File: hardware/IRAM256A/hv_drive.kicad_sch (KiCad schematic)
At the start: 21 parts

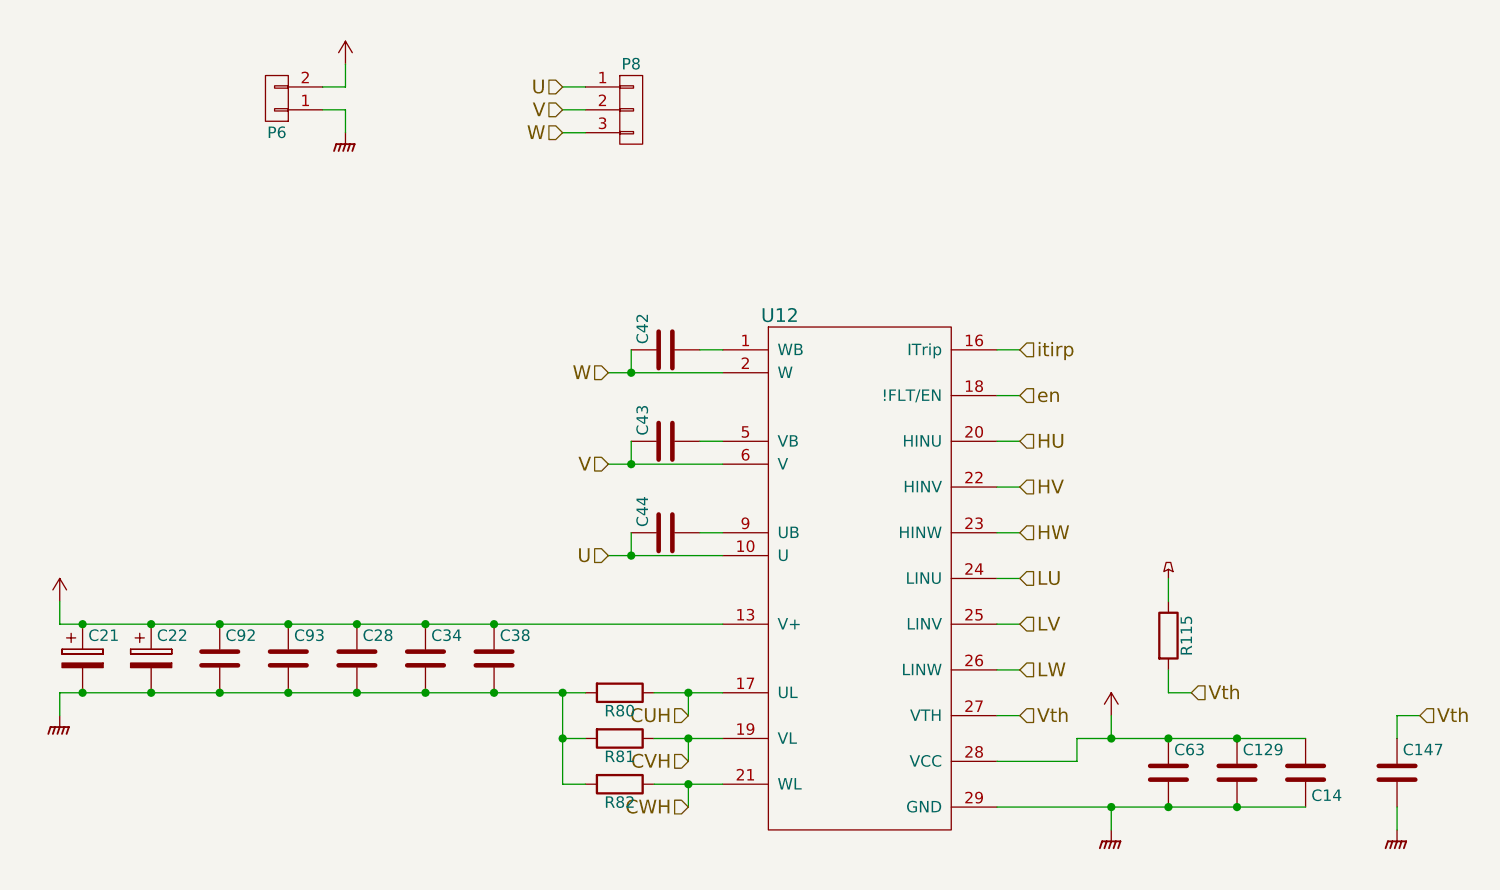
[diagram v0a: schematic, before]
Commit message: Structure change + kicad 3d models updated
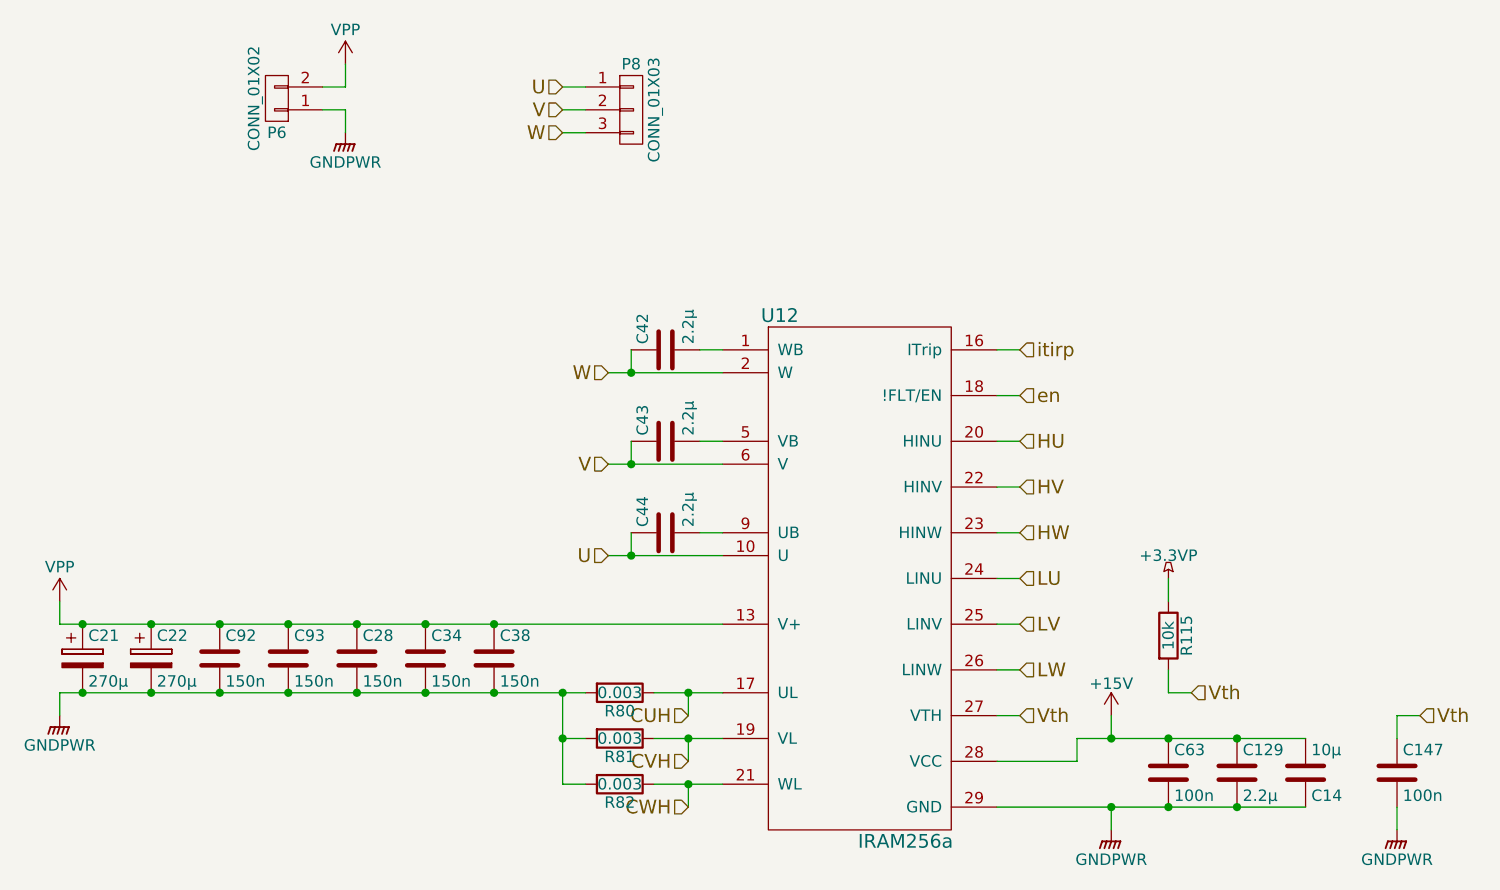
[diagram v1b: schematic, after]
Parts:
- C129, C42, C43, C44: value (none) -> 2.2µ; footprint (none) -> stmbl:C_0603
- C14: value (none) -> 10µ; footprint (none) -> stmbl:C_0805
- C147, C63: value (none) -> 100n; footprint (none) -> stmbl:C_0603
- C21, C22: value (none) -> 270µ; footprint (none) -> stmbl:C_Radial_D26_L45_P10
- C28, C34, C38, C92, C93: value (none) -> 150n; footprint (none) -> stmbl:C_1808
- P6: value (none) -> CONN_01X02; footprint (none) -> stmbl:RM5.08_1x2
- P8: value (none) -> CONN_01X03; footprint (none) -> stmbl:RM5.08_1x3
- R115: value (none) -> 10k; footprint (none) -> stmbl:R_0603
- R80, R81, R82: value (none) -> 0.003; footprint (none) -> stmbl:R_2512
- U12: value (none) -> IRAM256a; footprint (none) -> stmbl:IRAM256
